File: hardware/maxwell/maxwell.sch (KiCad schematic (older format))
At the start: 36 parts, among them J1 Canbus 1, J2 Canbus 2, J3 Neopixel, J4 Boot Selection Jumper, J5 Charger Output, J6 Programmer, Q1 BSS138, U1 MCP2515-E/ST-SOIC, U11 TPS2514, U2 SN65HVD233, U3 ITEAD_HC-05, U4 SIM800L_5-pin, U5 BOOST_BOARD, U6 STT3P2UH7, Y1 16M

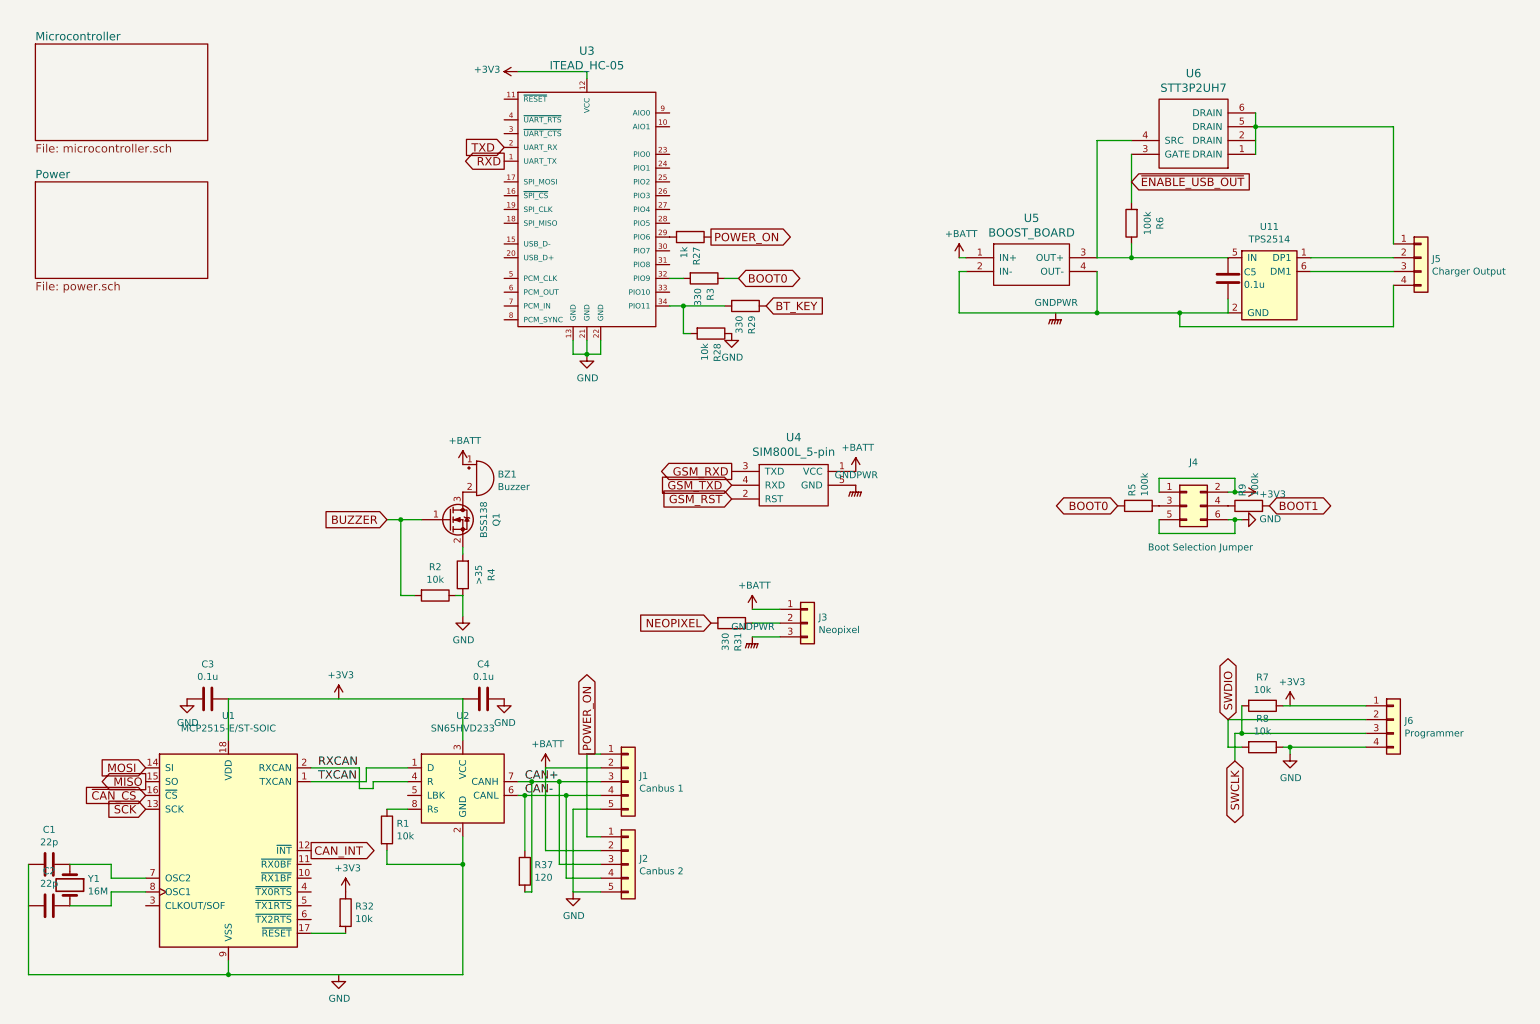
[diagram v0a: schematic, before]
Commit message: Updating schematic/layout to latest kicad version.
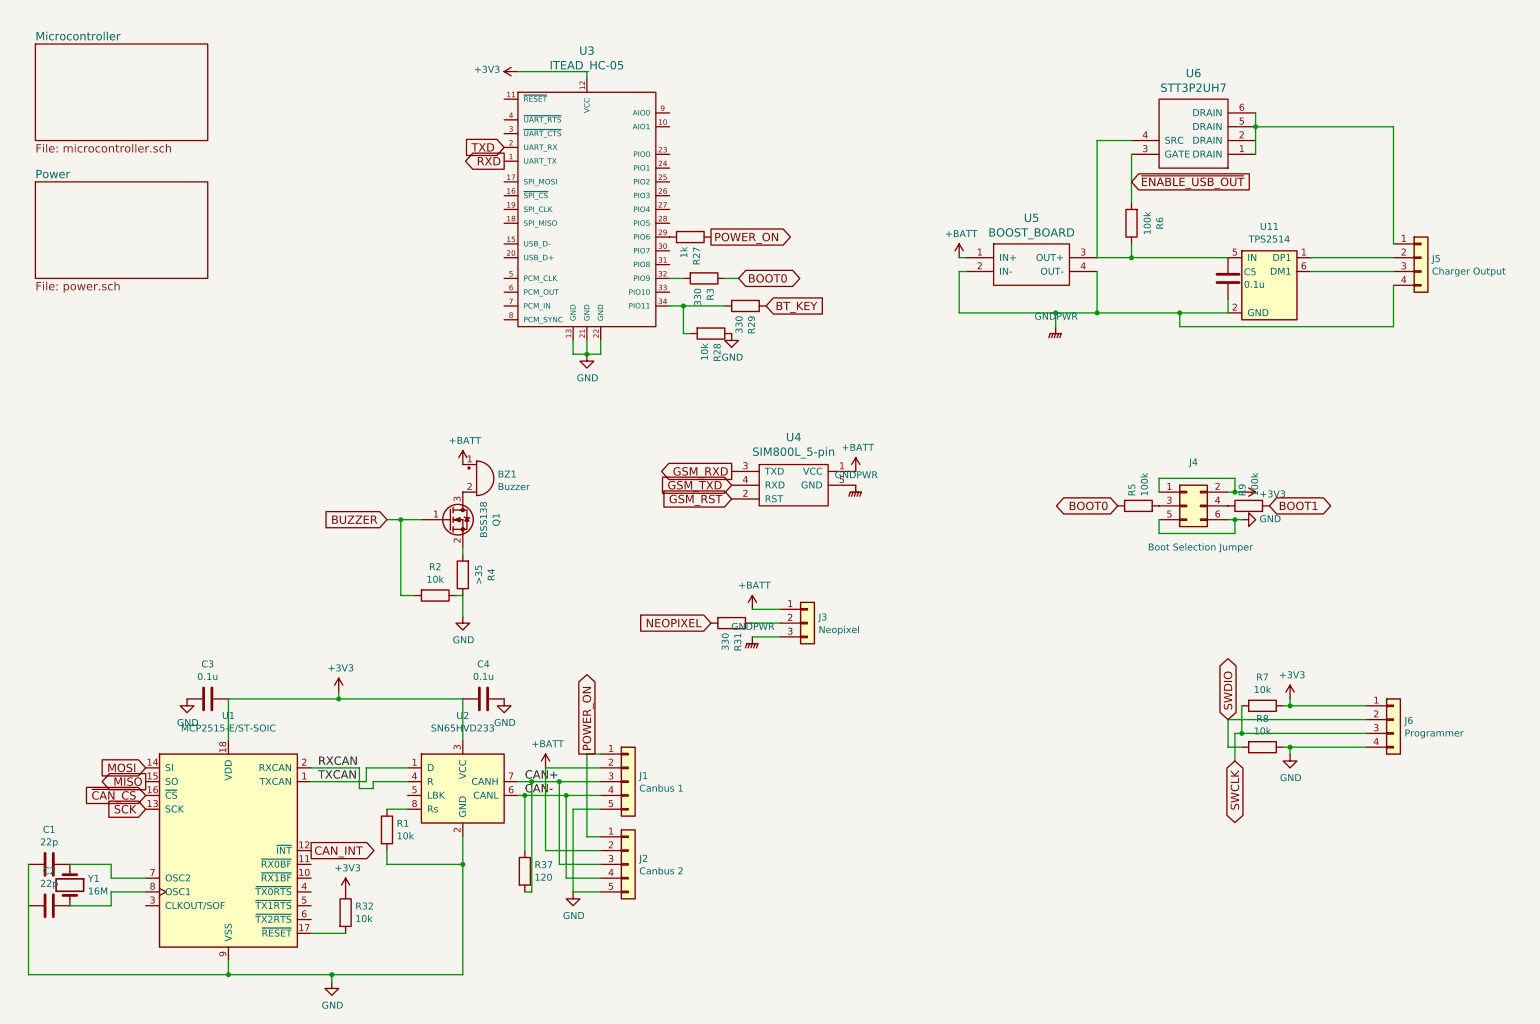
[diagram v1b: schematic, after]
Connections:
- net +3V3: now also C3.1, C4.2, J6.1 (Pin_1), R7.1, U1.18 (VDD), U2.3 (VCC)
- net GND: now also C1.1, R1.2, U1.9 (VSS), U2.2 (GND)
- net GNDPWR: now also C5.2, J5.4 (Pin_4), U11.2 (GND), U5.2 (IN-), U5.4 (OUT-)
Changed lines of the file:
@@
 L maxwell-rescue:+3V3-RESCUE-maxwell #PWR03
 U 1 1 5A178E3B
-P 9900 5550
-F 0 "#PWR03" H 9900 5400 50  0001 C CNN
-F 1 "+3V3" H 9915 5723 50  0000 C CNN
-F 2 "" H 9900 5550 50  0001 C CNN
-F 3 "" H 9900 5550 50  0001 C CNN
-	1    9900 5550
+P 9900 5500
+F 0 "#PWR03" H 9900 5350 50  0001 C CNN
+F 1 "+3V3" H 9915 5673 50  0000 C CNN
+F 2 "" H 9900 5500 50  0001 C CNN
+F 3 "" H 9900 5500 50  0001 C CNN
+	1    9900 5500
 	1    0    0    -1
 $EndComp
@@
 L maxwell-rescue:+3V3-RESCUE-maxwell #PWR07
 U 1 1 5A227CC0
-P 3000 5500
-F 0 "#PWR07" H 3000 5350 50  0001 C CNN
-F 1 "+3V3" H 3015 5673 50  0000 C CNN
-F 2 "" H 3000 5500 50  0001 C CNN
-F 3 "" H 3000 5500 50  0001 C CNN
-	1    3000 5500
+P 3000 5450
+F 0 "#PWR07" H 3000 5300 50  0001 C CNN
+F 1 "+3V3" H 3015 5623 50  0000 C CNN
+F 2 "" H 3000 5450 50  0001 C CNN
+F 3 "" H 3000 5450 50  0001 C CNN
+	1    3000 5450
 	1    0    0    -1
 $EndComp
@@
 L maxwell-rescue:GND-RESCUE-maxwell #PWR08
 U 1 1 5A22802C
-P 3000 7500
-F 0 "#PWR08" H 3000 7250 50  0001 C CNN
-F 1 "GND" H 3005 7327 50  0000 C CNN
-F 2 "" H 3000 7500 50  0001 C CNN
-F 3 "" H 3000 7500 50  0001 C CNN
-	1    3000 7500
+P 2950 7550
+F 0 "#PWR08" H 2950 7300 50  0001 C CNN
+F 1 "GND" H 2955 7377 50  0000 C CNN
+F 2 "" H 2950 7550 50  0001 C CNN
+F 3 "" H 2950 7550 50  0001 C CNN
+	1    2950 7550
 	1    0    0    -1
 $EndComp
@@
 L maxwell-rescue:GNDPWR-RESCUE-maxwell #PWR014
 U 1 1 5A29C476
-P 8200 2700
-F 0 "#PWR014" H 8200 2500 50  0001 C CNN
-F 1 "GNDPWR" H 8204 2774 50  0000 C CNN
-F 2 "" H 8200 2650 50  0001 C CNN
-F 3 "" H 8200 2650 50  0001 C CNN
-	1    8200 2700
+P 8200 2800
+F 0 "#PWR014" H 8200 2600 50  0001 C CNN
+F 1 "GNDPWR" H 8204 2874 50  0000 C CNN
+F 2 "" H 8200 2750 50  0001 C CNN
+F 3 "" H 8200 2750 50  0001 C CNN
+	1    8200 2800
 	1    0    0    -1
 $EndComp
@@
 	4400 6100 4600 6100
 Wire Wire Line
-	9850 5550 10450 5550
-Wire Wire Line
-	2200 5500 3900 5500
+	9850 5550 9900 5550
+Wire Wire Line
+	2200 5500 3000 5500
 Wire Wire Line
 	750  6700 750  7500
 Wire Wire Line
-	7500 2700 8500 2700
-Wire Wire Line
-	2200 7500 3900 7500
+	7500 2700 8200 2700
+Wire Wire Line
+	2200 7500 2950 7500
 Wire Wire Line
 	9650 1350 9650 1550
+Wire Wire Line
+	2950 7550 2950 7500
+Connection ~ 2950 7500
+Wire Wire Line
+	2950 7500 3900 7500
+Wire Wire Line
+	3000 5450 3000 5500
+Connection ~ 3000 5500
+Wire Wire Line
+	3000 5500 3900 5500
+Wire Wire Line
+	9900 5500 9900 5550
+Connection ~ 9900 5550
+Wire Wire Line
+	9900 5550 10450 5550
+Wire Wire Line
+	8200 2800 8200 2700
+Connection ~ 8200 2700
+Wire Wire Line
+	8200 2700 8500 2700
 $EndSCHEMATC

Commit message: Maxwell Board v2.0;
Adds:

* On-board P-MOS polarity protection.
* Adds On-board GPS (PA6C)
* Adds On-board WIFI, and BLE (ESP32)
* Connectors for 2x external UART devices.
* Connectors for 2x external SPI devices.
* Connector for I2C devices.

Removals:

* Removes on-board GSM; will add later via UART connectors mentioned
  above.
* Removes on-board boost charging.  Can later add this functionality via
  provided connectors.

Changes:

* Although the GNDPWR ground reference still exists, only neopixels
  are switched off via it.  The quiescent current of the GPS module
  and the ESP32 can be controlled via other means.
* Swaps many of the ICs used for switching and power regulation.
* Removes boot jumper bank.  I very rarely used it, and the HC-05
  has now been proven to work for switching boot modes for remote
  flashing.
* Removes natural powered-off state previously handled bydisabling the
  voltage regulator until POWER_ON was pulled high.  This will
  undoubtedly decrease how long the device will be able to operate due
  to increased quiescent currents, but I am willing to accept that given
  that removing that logic makes the design and software (especially
  around keeping the device on while flashing) simpler.
* Many other minor things.
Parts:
- removed C1, C2: 22p, coddingtonbear/coddingtonbear.pretty:0805_Milling, symbol maxwell-rescue:C-RESCUE-maxwell
- removed C3: 0.1u, coddingtonbear/coddingtonbear.pretty:0805_Milling, symbol maxwell-rescue:C-RESCUE-maxwell
- removed J4: Boot Selection Jumper, KiCad/Pin_Headers.pretty:Pin_Header_Straight_2x03_Pitch2.54mm, symbol maxwell-rescue:Conn_02x03_Odd_Even-RESCUE-maxwell
- removed J5: Charger Output, pbrook/Parts.pretty:JST-XH-4, symbol maxwell-rescue:Conn_01x04-RESCUE-maxwell
- removed R27: 1k, coddingtonbear/coddingtonbear.pretty:0805_Milling, symbol maxwell-rescue:R-RESCUE-maxwell
- removed R32: 10k, coddingtonbear/coddingtonbear.pretty:0805_Milling, symbol maxwell-rescue:R-RESCUE-maxwell
- removed U1: MCP2515-E/ST-SOIC, Tinkerforge/kicad-libraries:SOIC-18, symbol maxwell-rescue:MCP2515-E_ST-SOIC-RESCUE-maxwell
- removed U11: TPS2514, adamgreig/agg-kicad/agg.pretty:SOT-23-6, symbol maxwell-rescue:TPS2514-RESCUE-maxwell
- removed U4: SIM800L_5-pin, coddingtonbear/coddingtonbear.pretty:SIM800L_Breakout, symbol maxwell-rescue:SIM800L_5-pin-RESCUE-maxwell
- removed U5: BOOST_BOARD, coddingtonbear/coddingtonbear.pretty:BOOST_LM2596_3A, symbol maxwell-rescue:BOOST_BOARD-RESCUE-maxwell
- removed U6: STT3P2UH7, adamgreig/agg-kicad/agg.pretty:SOT-23-6, symbol maxwell-rescue:STT3P2UH7-RESCUE-maxwell
- removed Y1: 16M, SchrodingersGat/Components.pretty:crystal_hc-49s, symbol maxwell-rescue:Crystal-RESCUE-maxwell
- added J10: SPI2_B, coddingtonbear/coddingtonbear.pretty:JST_XH_B06B-XH-A_06x2.50mm_Straight_LargePads, symbol conn:Conn_01x06
- added J11: BACKUP, coddingtonbear/coddingtonbear.pretty:JST_XH_B02B-XH-A_02x2.50mm_Straight_LargePads, symbol conn:Conn_01x02
- added J12: UART4, coddingtonbear/coddingtonbear.pretty:JST_XH_B04B-XH-A_04x2.50mm_Straight_LargePads, symbol conn:Conn_01x04
- added J13: UART5, coddingtonbear/coddingtonbear.pretty:JST_XH_B04B-XH-A_04x2.50mm_Straight_LargePads, symbol conn:Conn_01x04
- added J14: I2C1, coddingtonbear/coddingtonbear.pretty:JST_XH_B04B-XH-A_04x2.50mm_Straight_LargePads, symbol conn:Conn_01x04
- added J4: BOOT0, coddingtonbear:Pin_Header_Straight_1x02_Pitch1.27mm_JMP, symbol conn:Conn_01x02
- added J5: SPI2_A, coddingtonbear/coddingtonbear.pretty:JST_XH_B06B-XH-A_06x2.50mm_Straight_LargePads, symbol conn:Conn_01x06
- added J8: BOOT1, coddingtonbear:Pin_Header_Straight_1x02_Pitch1.27mm_JMP, symbol conn:Conn_01x02
- added R16: 2.2k, coddingtonbear/coddingtonbear.pretty:0805_Milling, symbol maxwell-rescue:R-RESCUE-maxwell
- added U5: ESP-32S, coddingtonbear/coddingtonbear.pretty:ESP-32S, symbol esp32:ESP-32S
- added U6: FGPMMOPA6C, coddingtonbear/coddingtonbear.pretty:FGPMMOPA6C, symbol coddingtonbear-gps:FGPMMOPA6C
- J1, J2: footprint KiCad/Connectors_JST.pretty:JST_XH_B05B-XH-A_05x2.50mm_Straight -> coddingtonbear/coddingtonbear.pretty:JST_XH_B05B-XH-A_05x2.50mm_Straight_LargePads
- J3: footprint pbrook/Parts.pretty:JST-XH-3 -> coddingtonbear/coddingtonbear.pretty:JST_XH_B03B-XH-A_03x2.50mm_Straight_LargePads
- Q1: footprint adamgreig/agg-kicad/agg.pretty:SOT-23 -> coddingtonbear/coddingtonbear.pretty:SOT-23_LargePads
- R2: value 10k -> 2.2k
- R6: value 100k -> 10k
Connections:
- net labels added: +BACKUP, BT_DI, BT_DO, CAN_RX, CAN_TX, ESP_BOOT_MODE, ESP_DI, ESP_DO, GPS_DI, GPS_DO, I2C1_SCL, I2C1_SDA, SPI2_CS_A, SPI2_CS_B, SPI2_MISO, SPI2_MOSI, SPI2_SCK, UART4_RX, UART4_TX, UART5_RX, UART5_TX, ~DISABLE_ESP
- net labels removed: CAN_INT, GSM_RST, GSM_RXD, GSM_TXD, MISO, MOSI, RXCAN, RXD, SCK, TXCAN, TXD, ~CAN_CS, ~ENABLE_USB_OUT
- wire segments 124 -> 97
- no-connect marks 0 -> 60
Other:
- moved on the sheet: C4, J1, J2, J3, J6, R1, R31, R37, R7, R8, U2

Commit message: Updating for manufacture.
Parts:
- removed C5: 0.1u, coddingtonbear/coddingtonbear.pretty:0805_Milling, symbol maxwell-rescue:C-RESCUE-maxwell
- removed R28: 10k, coddingtonbear/coddingtonbear.pretty:0805_Milling, symbol maxwell-rescue:R-RESCUE-maxwell
- removed R29, R3: 330, coddingtonbear/coddingtonbear.pretty:0805_Milling, symbol maxwell-rescue:R-RESCUE-maxwell
- removed U3: ITEAD_HC-05, pelrun/libKiCad/footprint/w_rf_modules.pretty:ITEAD_HC-05, symbol maxwell-rescue:ITEAD_HC-05-RESCUE-maxwell
- removed U6: FGPMMOPA6C, coddingtonbear/coddingtonbear.pretty:FGPMMOPA6C, symbol coddingtonbear-gps:FGPMMOPA6C
- added C5: 0.1u, coddingtonbear/coddingtonbear.pretty:0805_Milling, symbol device:C
- added J16: ESP_BM, coddingtonbear/coddingtonbear.pretty:Pin_Header_Straight_1x02_Pitch1.27mm_JMP, symbol conn:Conn_01x02
- added J17: ESP_PROG, coddingtonbear/coddingtonbear.pretty:JST_XH_B03B-XH-A_03x2.50mm_Straight_LargePads, symbol maxwell-rescue:Conn_01x03-RESCUE-maxwell
- U5: symbol esp32:ESP-32S -> maxwell-rescue:ESP-32S-esp32
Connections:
- net labels added: CAN_DISABLE, N_RST, VCC
- net labels removed: +BATT, GPS_DI, GPS_DO
- wire segments 97 -> 88
- no-connect marks 60 -> 26

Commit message: Updating hardware design.
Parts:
- C5: symbol device:C -> maxwell-rescue:C-device
- J10, J5: symbol conn:Conn_01x06 -> maxwell-rescue:Conn_01x06-conn
- J11, J16, J4, J8: symbol conn:Conn_01x02 -> maxwell-rescue:Conn_01x02-conn
- J12, J13, J14: symbol conn:Conn_01x04 -> maxwell-rescue:Conn_01x04-conn
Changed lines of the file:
@@
 $EndComp
 $Comp
-L conn:Conn_01x02 J4
+L maxwell-rescue:Conn_01x02-conn J4
 U 1 1 5A8A1BD4
 P 3250 1100
@@
 $EndComp
 $Comp
-L conn:Conn_01x02 J8
+L maxwell-rescue:Conn_01x02-conn J8
 U 1 1 5A8A1C87
 P 3250 2350
@@
 SPI2_MISO
 $Comp
-L conn:Conn_01x06 J5
+L maxwell-rescue:Conn_01x06-conn J5
 U 1 1 5A872F71
 P 7950 1550
@@
 $EndComp
 $Comp
-L conn:Conn_01x06 J10
+L maxwell-rescue:Conn_01x06-conn J10
 U 1 1 5A87305D
 P 8350 1550
@@
 	3350 4200 3600 4200
 $Comp
-L conn:Conn_01x02 J11
+L maxwell-rescue:Conn_01x02-conn J11
 U 1 1 5A8ACC4B
 P 2550 2050
@@
 $EndComp
 $Comp
-L conn:Conn_01x04 J12
+L maxwell-rescue:Conn_01x04-conn J12
 U 1 1 5A8B4267
 P 4450 5700
@@
 $EndComp
 $Comp
-L conn:Conn_01x04 J13
+L maxwell-rescue:Conn_01x04-conn J13
 U 1 1 5A8B42C9
 P 4450 6200
@@
 I2C1_SCL
 $Comp
-L conn:Conn_01x04 J14
+L maxwell-rescue:Conn_01x04-conn J14
 U 1 1 5A8B5837
 P 5800 5750
@@
 N_RST
 $Comp
-L device:C C5
+L maxwell-rescue:C-device C5
 U 1 1 5B327200
 P 7900 2750
@@
 ESP_BOOT_MODE
 $Comp
-L conn:Conn_01x02 J16
+L maxwell-rescue:Conn_01x02-conn J16
 U 1 1 5B336731
 P 5500 2100
